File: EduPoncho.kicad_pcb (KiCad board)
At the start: 2 copper layers, 88.5 x 137.5 mm, 44 parts, among them J1 TB_1X3, J2 TB_1X3, J3 TB_1X3, Q1 NDS7002A, Q2 NDS7002A, Q3 BC849, U1 PS2805-1, U2 PS2805-1, U3 CNY70, U4 Buzzer

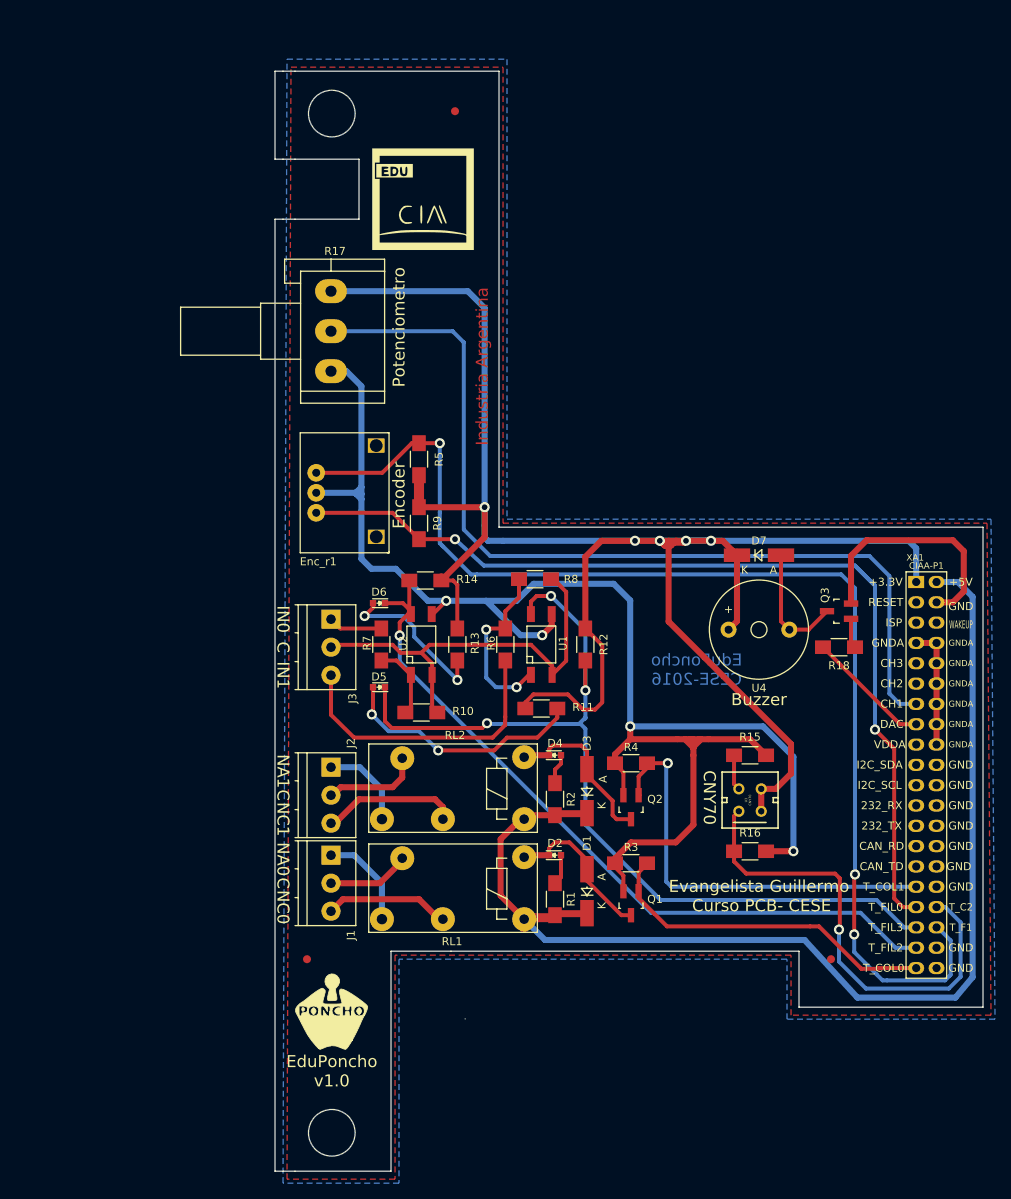
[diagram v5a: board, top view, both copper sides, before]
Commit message: Reubicacion de optoacopladores, cambio de footoprins de resistencias a 0805, correcion general.Falta arreglar archivos vista 3d y completar los campos #digikey
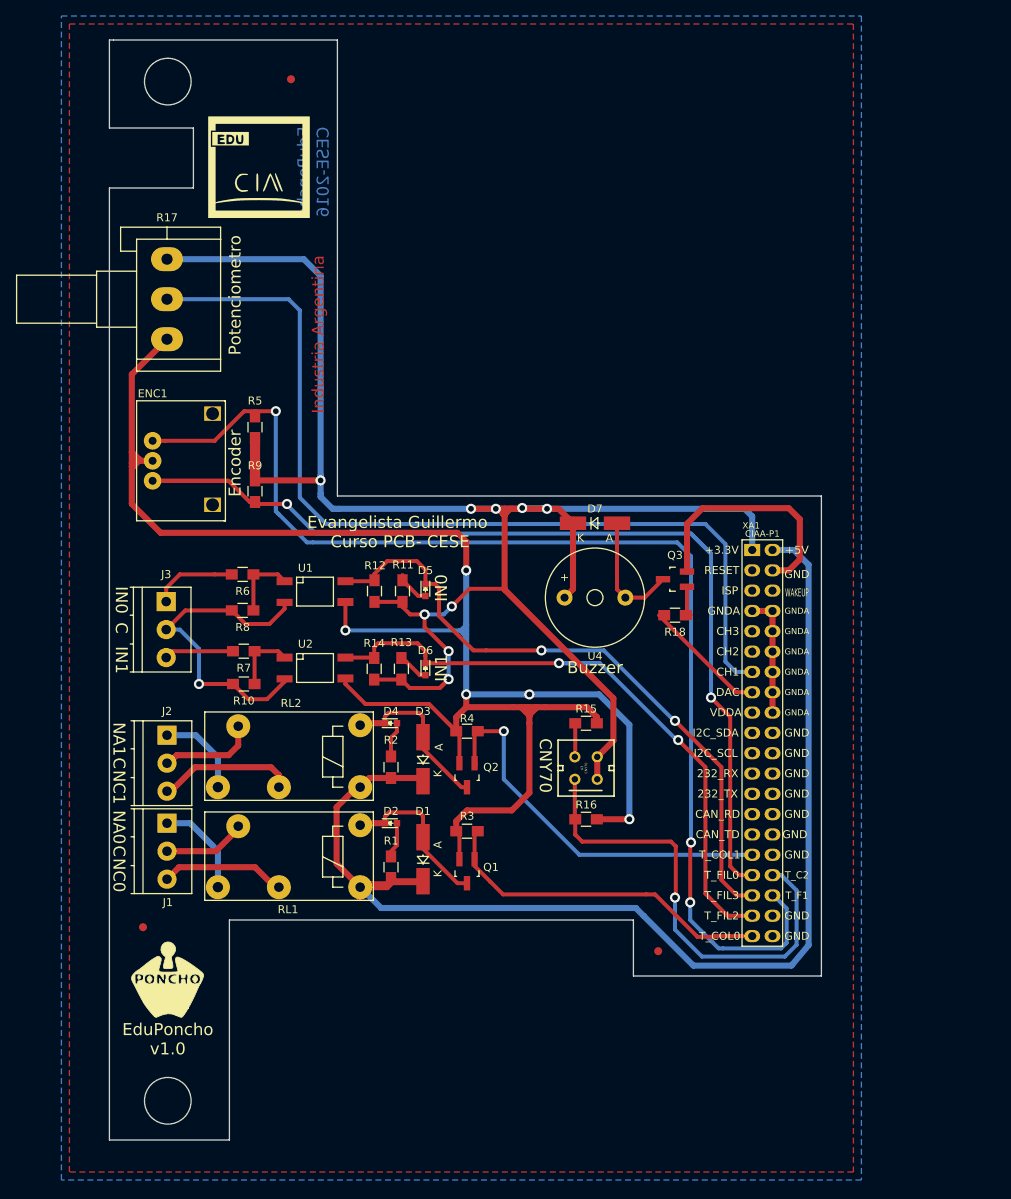
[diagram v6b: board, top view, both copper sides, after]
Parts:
- removed Enc_r1: Encoder_rotativo, Potentiometers:Potentiometer_Alps-RK16-single_largePads
- added ENC1: Encoder_rotativo, footprint:Encoder_rotativo, F.Cu at (57.4, 78.1)
- R1, R10, R11, R12, R13, R14, R15, R16, R18, R2, R3, R4, R5, R6, R7, R8, R9: footprint Resistors_SMD:R_1206_HandSoldering -> Resistors_SMD:R_0805_HandSoldering
- moved R8 36.8 mm to (68.7, 96.8), turned to 180 degrees
- moved R6 34.0 mm to (68.7, 92.3), turned to 180 degrees
- moved U1 29.1 mm to (77.7, 94.5), turned to 0 degrees
- moved R12 27.2 mm to (85.1, 94.4), turned to 90 degrees
- moved R11 22.7 mm to (88.6, 94.4), turned to 90 degrees
- moved R10 22.5 mm to (68.8, 106.0), turned to 180 degrees
- moved F? 21.6 mm to (120.6, 139.4)
- moved R15 20.9 mm to (111.6, 110.9)
- moved R16 20.9 mm to (111.6, 122.9)
- moved U3 20.9 mm to (111.6, 116.5)
- moved R17 20.9 mm to (59.2, 62.9)
- moved D1 20.9 mm to (91.2, 127.9)
- moved D2 20.9 mm to (87.2, 123.4)
- moved D3 20.9 mm to (91.2, 115.4)
- moved D4 20.9 mm to (87.2, 110.9)
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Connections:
- D5 pad 1: /Conector Poncho/OPTO_IN1 -> /Conector Poncho/OPTO_IN0
- D6 pad 1: /Conector Poncho/OPTO_IN0 -> /Conector Poncho/OPTO_IN1
- R12 pad 2: /Conector Poncho/OPTO_IN1 -> /Conector Poncho/OPTO_IN0
- R14 pad 2: /Conector Poncho/OPTO_IN0 -> /Conector Poncho/OPTO_IN1
- R6 pad 2: /Entradas/IN1 -> /Entradas/IN0
- R7 pad 2: /Entradas/IN0 -> /Entradas/IN1
- U1 pad 4: /Conector Poncho/OPTO_IN1 -> /Conector Poncho/OPTO_IN0
- U2 pad 4: /Conector Poncho/OPTO_IN0 -> /Conector Poncho/OPTO_IN1
- XA1 pad 35: /Conector Poncho/OPTO_IN1 -> /Conector Poncho/OPTO_IN0
- XA1 pad 37: /Conector Poncho/OPTO_IN0 -> /Conector Poncho/OPTO_IN1
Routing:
- net /Conector Poncho/OPTO_IN1: track 115.3 -> 81.8 mm, vias 3 -> 2
- net /Entradas/IN1: track 36.6 -> 8.68 mm
- net Net-(D5-Pad2): track 31.4 -> 4.33 mm, vias 2 -> 0
- net GND: track 228.2 -> 255.2 mm, vias 4 -> 5
- net +3V3: track 283.1 -> 263.0 mm, vias 5 -> 9
- net Net-(D6-Pad2): track 20.1 -> 3.89 mm, vias 2 -> 0
- net /Conector Poncho/OPTO_IN0: track 94.4 -> 80.4 mm, vias 1 -> 2
- net /Entradas/COM: track 52.7 -> 39.0 mm, vias 0 -> 1
- net Net-(R6-Pad1): track 22.0 -> 8.75 mm, vias 2 -> 0
- net /Conector Poncho/Encoder_A: track 120.5 -> 130.1 mm
- net /Conector Poncho/GPIO1: track 53.6 -> 47.9 mm
- net +5V: track 160.6 -> 157.0 mm
- net /Entradas/IN0: track 6.77 -> 9.95 mm
- net Net-(D1-Pad2): track 20.3 -> 22.4 mm
- net Net-(R10-Pad1): track 9.43 -> 8.18 mm
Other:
- board size 88.5 x 137.5 mm -> 89 x 137.5 mm

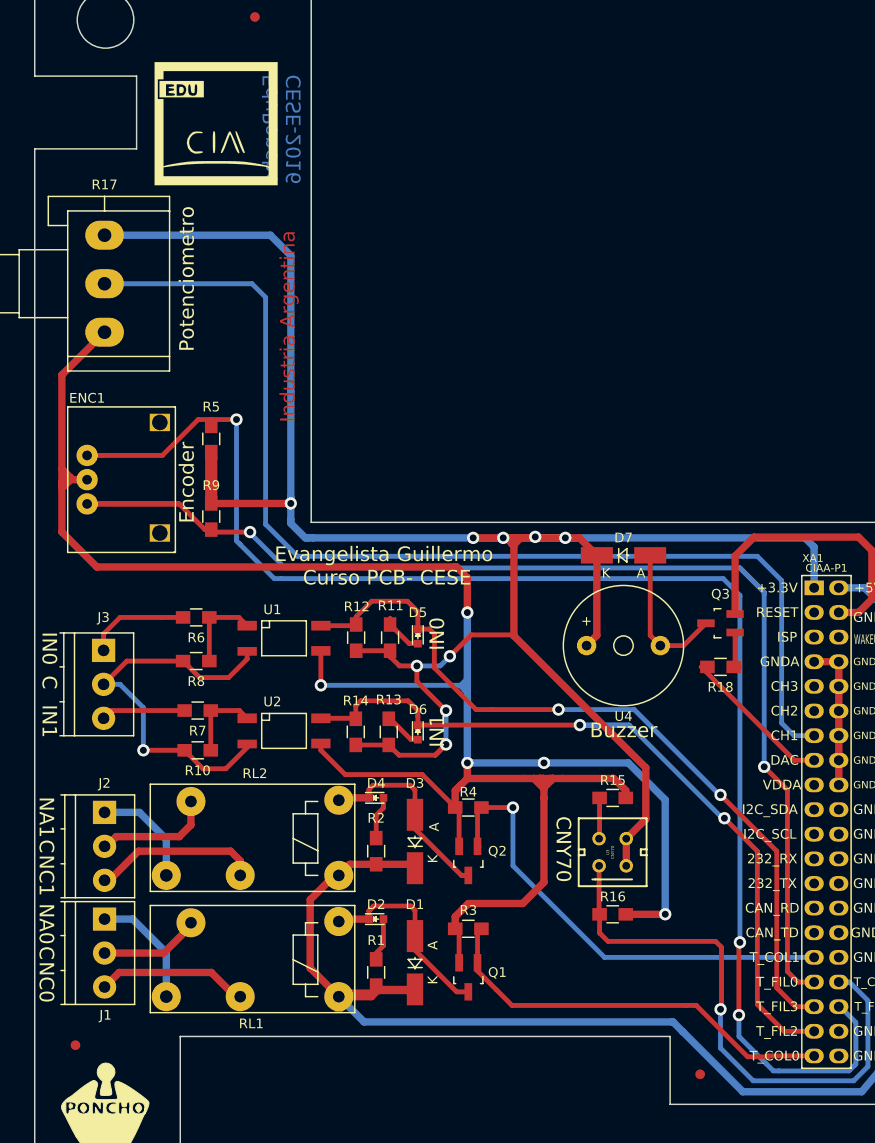
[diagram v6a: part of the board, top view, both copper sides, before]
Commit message: Se agrego documentacion del proyecto, se agregaron vistas 3d faltantes y se repararon las extensiones de las que no funcionaban
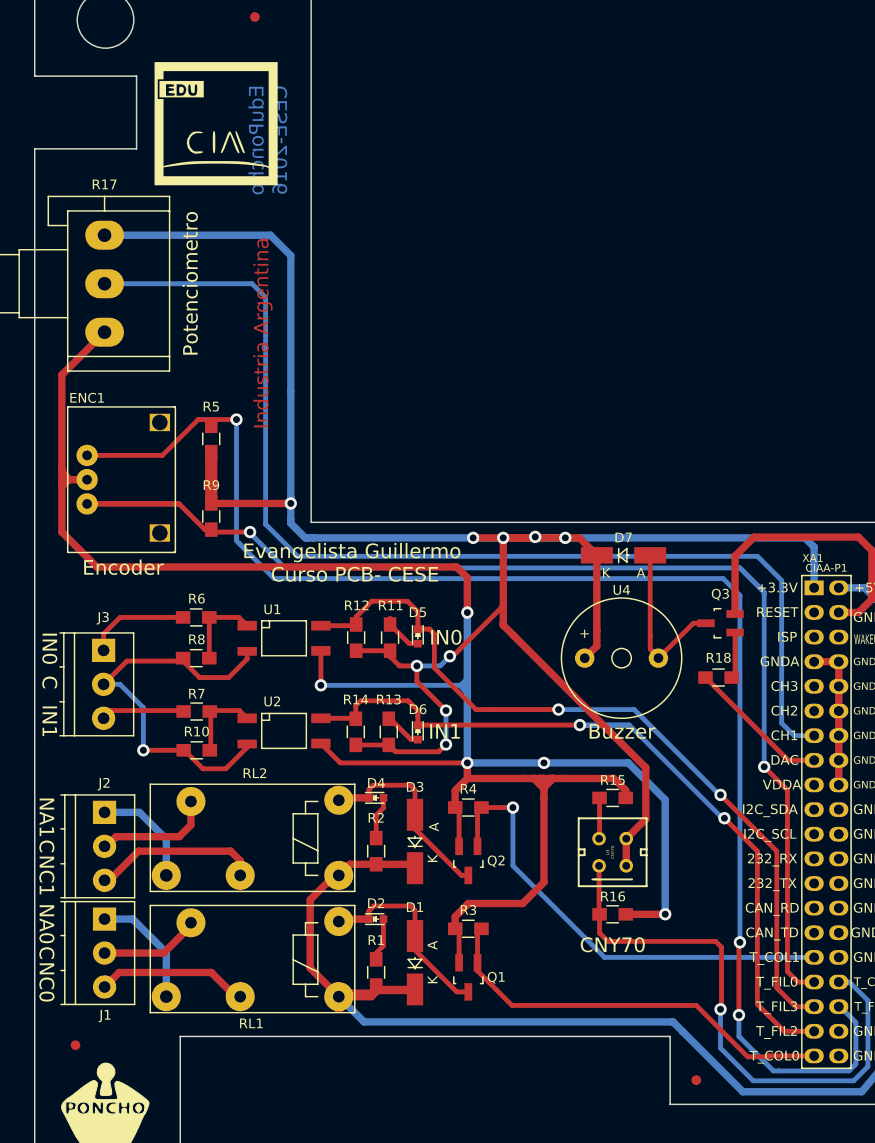
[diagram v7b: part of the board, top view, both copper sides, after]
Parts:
- moved U4 1.31 mm to (112.5, 96.5)
- moved R18 1.12 mm to (122.5, 98.5)
- moved F? 0.72 mm to (120.2, 140.0)
- moved R8 0.30 mm to (68.7, 96.5)
- moved R7 0.14 mm to (68.7, 102.0)
- moved R10 0.10 mm to (68.7, 106.0)
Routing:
- net +3V3: track 263.0 -> 260.3 mm
- net GND: track 255.2 -> 252.8 mm
- net Net-(D7-Pad2): track 15.4 -> 17.3 mm
- net Net-(Q3-Pad1): track 3.76 -> 4.80 mm
- net /Conector Poncho/Buzzer: track 15.6 -> 14.7 mm
